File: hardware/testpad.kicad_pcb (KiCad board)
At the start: 4 copper layers, 54.5 x 93.2 mm, 51 parts, among them J1 HC-TYPE-C-16P-CB1.6, J3 AFA01-S08FCA-00, SW1 SSSS811101, SW2 SC4823S6-TR, SW3 SC4823S6-TR, SW4 SC4823S6-TR, SW5 SC4823S6-TR, T1 XL4067TS, U1 ESP32-C6-WROOM-1-N8, U2 BQ24074RGTR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

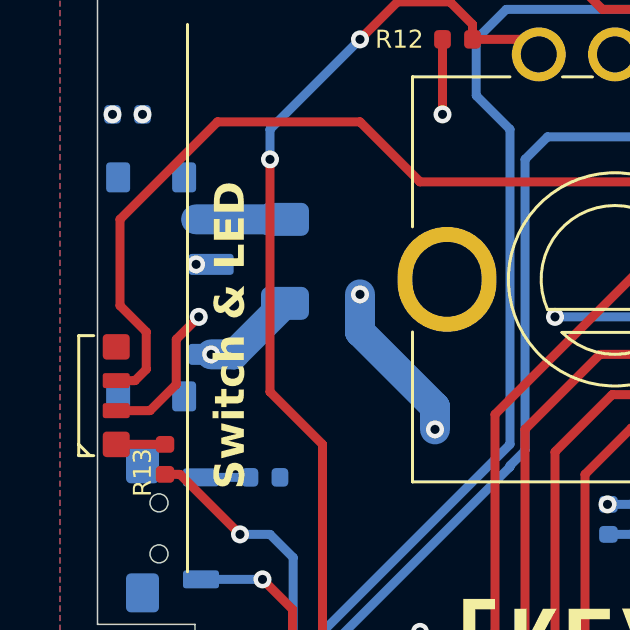
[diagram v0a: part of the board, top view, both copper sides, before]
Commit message: :bug: fix switch hole
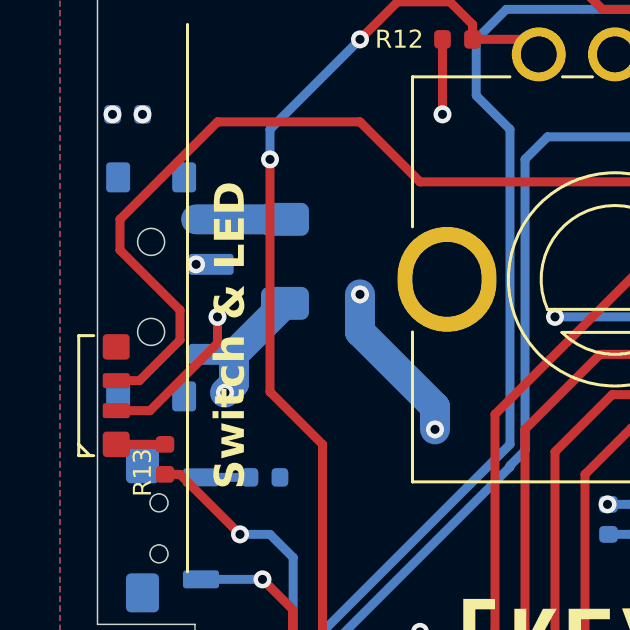
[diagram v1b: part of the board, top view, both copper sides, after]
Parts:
- J3: value AFA01-S08FCA-00 -> AFA01S08FCA00
- PC1: value HC-1.25-4PWT -> HC-1.25-2PWT
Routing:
- net /TOMO0: track 117.7 -> 118.8 mm

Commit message: :construction: panelize all boards
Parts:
- J3: value AFA01S08FCA00 -> AFA01-S08FCA-00
- PC1: value HC-1.25-2PWT -> HC-1.25-4PWT
